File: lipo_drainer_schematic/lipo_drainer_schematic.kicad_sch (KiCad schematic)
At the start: 57 parts, among them J1 BATT, J2 FAN, J3 Vcal, J4 128x64_OLED, J5 Gcal, J6 Ical, Q1 MMBT3904, Q10 G700P06T, Q11 G700P06T, Q2 IRLML5103TRPBF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

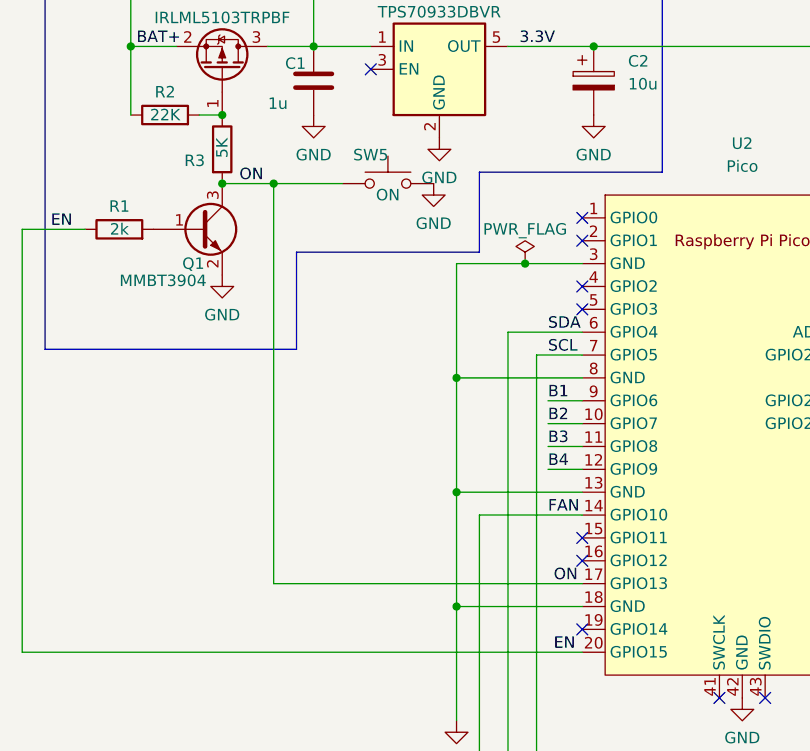
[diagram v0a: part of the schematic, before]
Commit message: Removed ineffective ON button
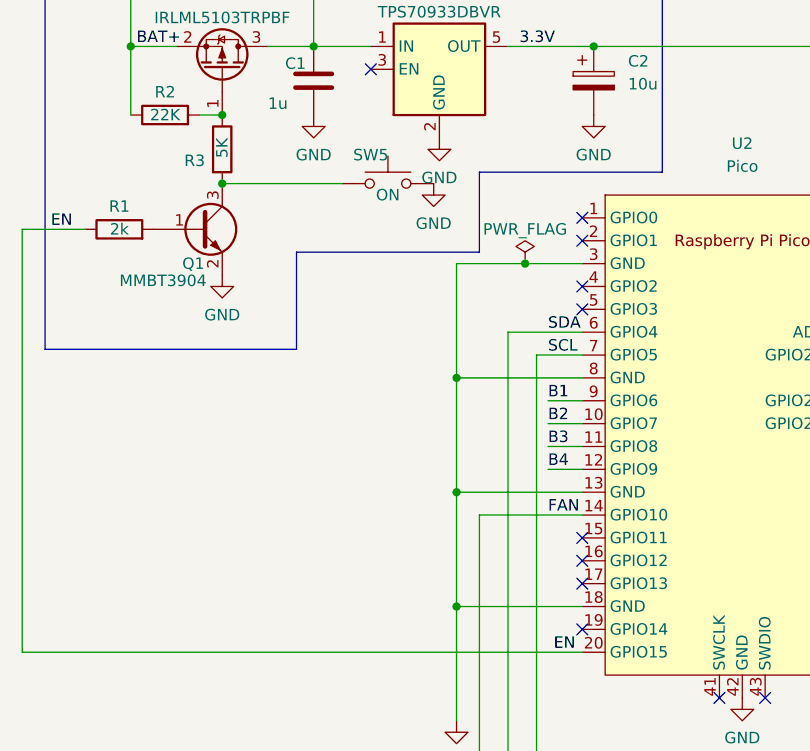
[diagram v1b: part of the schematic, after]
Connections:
- net ON: no longer names the net of Q1.3 (C), R3.2, SW5.1
- net ON: no longer U2.17 (GPIO13)
- no-connect marks 18 -> 19
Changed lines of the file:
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@@
   (junction (at 144.145 118.11) (diameter 0) (color 0 0 0 0)
-  )
-  (junction (at 72.39 71.12) (diameter 0) (color 0 0 0 0)
   )
   (junction (at 258.445 59.055) (diameter 0) (color 0 0 0 0)
@@
   (no_connect (at 142.24 102.87))
   (no_connect (at 142.24 90.17))
+  (no_connect (at 106.68 115.57))
   (no_connect (at 127 128.27))
   (no_connect (at 106.68 113.03))
@@
     (stroke (width 0) (type default))
   )
-  (wire (pts (xy 72.39 115.57) (xy 72.39 71.12))
-    (stroke (width 0) (type default))
-  )
   (polyline (pts (xy 193.675 93.98) (xy 240.665 93.98))
     (stroke (width 0) (type default))
@@
     (stroke (width 0) (type default))
   )
-  (wire (pts (xy 72.39 71.12) (xy 80.01 71.12))
+  (wire (pts (xy 66.675 71.12) (xy 80.01 71.12))
     (stroke (width 0) (type default))
   )
@@
     (stroke (width 0) (type default))
   )
-  (wire (pts (xy 106.68 115.57) (xy 72.39 115.57))
-    (stroke (width 0) (type default))
-  )
   (wire (pts (xy 174.625 39.37) (xy 174.625 43.815))
     (stroke (width 0) (type default))
@@
   )
   (wire (pts (xy 144.145 118.11) (xy 142.24 118.11))
-    (stroke (width 0) (type default))
-  )
-  (wire (pts (xy 66.675 71.12) (xy 72.39 71.12))
     (stroke (width 0) (type default))
   )
@@
     (effects (font (size 1.27 1.27)) (justify left bottom))
   )
-  (label "ON" (at 68.58 71.12 0) (fields_autoplaced)
-    (effects (font (size 1.27 1.27)) (justify left bottom))
-  )
   (label "BAT+" (at 57.15 55.88 0) (fields_autoplaced)
     (effects (font (size 1.27 1.27)) (justify left bottom))
@@
     (effects (font (size 1.27 1.27)) (justify left bottom))
   )
-  (label "ON" (at 103.505 115.57 0) (fields_autoplaced)
-    (effects (font (size 1.27 1.27)) (justify left bottom))
-  )

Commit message: Started work on layout
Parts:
- added R25: 100k, Resistor_SMD:R_0805_2012Metric_Pad1.20x1.40mm_HandSolder, symbol Device:R
- J1: footprint (none) -> Connector_AMASS:AMASS_XT60-M_1x02_P7.20mm_Vertical
- U2: footprint RPi_Pico:RPi_Pico_SMD_TH -> MCU_RaspberryPi_and_Boards:RPi_Pico_SMD_TH
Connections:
- net GND: now also R25.1
- net at C4.1, J5.2 (Pin_2), Q10.1 (G)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: now also R25.2
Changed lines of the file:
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@@
   (junction (at 258.445 59.055) (diameter 0) (color 0 0 0 0)
+  )
+  (junction (at 253.365 66.675) (diameter 0) (color 0 0 0 0)
   )
   (junction (at 127 43.815) (diameter 0) (color 0 0 0 0)
@@
       (effects (font (size 1.27 1.27)) (justify right))
     )
-    (property "Footprint" "" (at 24.13 29.845 0)
+    (property "Footprint" "Connector_AMASS:AMASS_XT60-M_1x02_P7.20mm_Vertical" (at 24.13 29.845 0)
       (effects (font (size 1.27 1.27)) hide)
     )
@@
         (path "/db6692d0-0595-40e8-a350-9f6ef4d6e67d"
           (reference "#PWR06") (unit 1)
+        )
+      )
+    )
+  )
+  (symbol (lib_id "power:GND") (at 253.365 74.295 0) (unit 1)
+    (in_bom yes) (on_board yes) (dnp no) (fields_autoplaced)
+    (property "Reference" "#PWR018" (at 253.365 80.645 0)
+      (effects (font (size 1.27 1.27)) hide)
+    )
+    (property "Value" "GND" (at 253.365 78.74 0)
+      (effects (font (size 1.27 1.27)))
+    )
+    (property "Footprint" "" (at 253.365 74.295 0)
+      (effects (font (size 1.27 1.27)) hide)
+    )
+    (property "Datasheet" "" (at 253.365 74.295 0)
+      (effects (font (size 1.27 1.27)) hide)
+    )
+    (pin "1")
+    (instances
+      (project "lipo_drainer_schematic"
+        (path "/db6692d0-0595-40e8-a350-9f6ef4d6e67d"
+          (reference "#PWR018") (unit 1)
         )
       )
@@
       (effects (font (size 1.27 1.27)))
     )
-    (property "Footprint" "RPi_Pico:RPi_Pico_SMD_TH" (at 124.46 99.06 90)
+    (property "Footprint" "MCU_RaspberryPi_and_Boards:RPi_Pico_SMD_TH" (at 124.46 99.06 90)
       (effects (font (size 1.27 1.27)) hide)
     )
@@
         )
       )
+    )
+  )
+  (symbol (lib_id "Device:R") (at 253.365 70.485 180) (unit 1)
+    (in_bom yes) (on_board yes) (dnp no)
+    (property "Reference" "R25" (at 250.825 70.485 90)
+      (effects (font (size 1.27 1.27)))
+    )
+    (property "Value" "100k" (at 253.365 70.485 90)
+      (effects (font (size 1.27 1.27)))
+    )
+    (property "Footprint" "Resistor_SMD:R_0805_2012Metric_Pad1.20x1.40mm_HandSolder" (at 255.143 70.485 90)
+      (effects (font (size 1.27 1.27)) hide)
+    )
+    (property "Datasheet" "~" (at 253.365 70.485 0)
+      (effects (font (size 1.27 1.27)) hide)
+    )
+    (pin "1")
+    (pin "2")
+    (instances
+      (project "lipo_drainer_schematic"
+        (path "/db6692d0-0595-40e8-a350-9f6ef4d6e67d"
+          (reference "R25") (unit 1)
+        )
+      )

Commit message: Added temperature sensor
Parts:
- added J7: Heatsink Temp (for MCP7901), Connector_PinHeader_2.54mm:PinHeader_1x03_P2.54mm_Vertical, symbol Connector:Conn_01x03_Pin
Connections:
- net GND: now also J7.1 (Pin_1)
- net 3V3: now reaches R7.2, U2.36 (3V3)
- net 3V3: now also J4.1 (Pin_1), J7.2 (Pin_2)
- net TEMP: now reaches U2.34 (GPIO28_ADC2)
- net TEMP: now also J7.3 (Pin_3)
- net 3.3V renamed VSYS
- net VSYS: no longer J4.1 (Pin_1)
- net ADC renamed VOLT
- no-connect marks 19 -> 18
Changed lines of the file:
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@@
   (no_connect (at 83.185 58.42))
   (no_connect (at 142.24 102.87))
-  (no_connect (at 142.24 90.17))
   (no_connect (at 106.68 115.57))
   (no_connect (at 127 128.27))
@@
     (stroke (width 0) (type default))
   )
+  (wire (pts (xy 150.495 90.17) (xy 150.495 133.35))
+    (stroke (width 0) (type default))
+  )
   (wire (pts (xy 225.425 66.675) (xy 238.76 66.675))
     (stroke (width 0) (type default))
@@
     (stroke (width 0) (type default))
   )
+  (wire (pts (xy 150.495 135.89) (xy 154.94 135.89))
+    (stroke (width 0) (type default))
+  )
   (wire (pts (xy 138.43 162.56) (xy 149.86 162.56))
     (stroke (width 0) (type default))
@@
     (stroke (width 0) (type default))
   )
+  (wire (pts (xy 142.24 90.17) (xy 150.495 90.17))
+    (stroke (width 0) (type default))
+  )
   (wire (pts (xy 138.43 160.02) (xy 138.43 162.56))
     (stroke (width 0) (type default))
@@
   )
   (wire (pts (xy 92.71 118.11) (xy 92.71 130.81))
+    (stroke (width 0) (type default))
+  )
+  (wire (pts (xy 150.495 133.35) (xy 154.94 133.35))
     (stroke (width 0) (type default))
   )
@@
     (effects (font (size 1.27 1.27)) (justify left bottom))
   )
-  (label "3.3V" (at 149.225 77.47 0) (fields_autoplaced)
+  (label "VSYS" (at 146.05 77.47 0) (fields_autoplaced)
     (effects (font (size 1.27 1.27)) (justify left bottom))
   )
@@
     (effects (font (size 1.27 1.27)) (justify left bottom))
   )
-  (label "ADC" (at 178.435 67.945 0) (fields_autoplaced)
+  (label "VOLT" (at 178.435 67.945 0) (fields_autoplaced)
     (effects (font (size 1.27 1.27)) (justify left bottom))
   )
@@
     (effects (font (size 1.27 1.27)) (justify left bottom))
   )
-  (label "FAST" (at 146.685 123.19 0) (fields_autoplaced)
+  (label "FAST" (at 144.78 123.19 0) (fields_autoplaced)
     (effects (font (size 1.27 1.27)) (justify left bottom))
   )
@@
     (effects (font (size 1.27 1.27)) (justify left bottom))
   )
-  (label "ADC" (at 149.86 97.79 0) (fields_autoplaced)
+  (label "VOLT" (at 149.225 97.79 0) (fields_autoplaced)
     (effects (font (size 1.27 1.27)) (justify left bottom))
   )
@@
     (effects (font (size 1.27 1.27)) (justify left bottom))
   )
+  (label "TEMP" (at 145.415 90.17 0) (fields_autoplaced)
+    (effects (font (size 1.27 1.27)) (justify left bottom))
+  )
   (label "EN" (at 103.505 123.19 0) (fields_autoplaced)
     (effects (font (size 1.27 1.27)) (justify left bottom))
@@
     (effects (font (size 1.27 1.27)) (justify left bottom))
   )
+  (label "3V3" (at 145.415 85.09 0) (fields_autoplaced)
+    (effects (font (size 1.27 1.27)) (justify left bottom))
+  )
   (label "B1" (at 102.87 95.25 0) (fields_autoplaced)
     (effects (font (size 1.27 1.27)) (justify left bottom))
   )
-  (label "SLOW" (at 146.685 120.65 0) (fields_autoplaced)
+  (label "TEMP" (at 150.495 133.35 0) (fields_autoplaced)
+    (effects (font (size 1.27 1.27)) (justify left bottom))
+  )
+  (label "SLOW" (at 144.78 120.65 0) (fields_autoplaced)
     (effects (font (size 1.27 1.27)) (justify left bottom))
   )
@@
     (effects (font (size 1.27 1.27)) (justify left bottom))
   )
+  (label "3V3" (at 150.495 135.89 0) (fields_autoplaced)
+    (effects (font (size 1.27 1.27)) (justify left bottom))
+  )
   (label "3V" (at 151.13 87.63 0) (fields_autoplaced)
     (effects (font (size 1.27 1.27)) (justify left bottom))
@@
     (effects (font (size 1.27 1.27)) (justify left bottom))
   )
-  (label "3.3V" (at 99.695 55.88 0) (fields_autoplaced)
-    (effects (font (size 1.27 1.27)) (justify left bottom))
-  )
-  (label "3.3V" (at 219.075 135.255 0) (fields_autoplaced)
+  (label "VSYS" (at 99.695 55.88 0) (fields_autoplaced)
+    (effects (font (size 1.27 1.27)) (justify left bottom))
+  )
+  (label "3V3" (at 219.075 135.255 0) (fields_autoplaced)
     (effects (font (size 1.27 1.27)) (justify left bottom))
   )
@@
         (path "/db6692d0-0595-40e8-a350-9f6ef4d6e67d"
           (reference "Q7") (unit 1)
+        )
+      )
+    )
+  )
+  (symbol (lib_id "Connector:Conn_01x03_Pin") (at 160.02 135.89 180) (unit 1)
+    (in_bom yes) (on_board yes) (dnp no) (fields_autoplaced)
+    (property "Reference" "J7" (at 161.29 135.255 0)
+      (effects (font (size 1.27 1.27)) (justify right))
+    )
+    (property "Value" "Heatsink Temp (for MCP7901)" (at 161.29 137.795 0)
+      (effects (font (size 1.27 1.27)) (justify right))
+    )
+    (property "Footprint" "Connector_PinHeader_2.54mm:PinHeader_1x03_P2.54mm_Vertical" (at 160.02 135.89 0)
+      (effects (font (size 1.27 1.27)) hide)
+    )
+    (property "Datasheet" "~" (at 160.02 135.89 0)
+      (effects (font (size 1.27 1.27)) hide)
+    )
+    (pin "1")
+    (pin "2")
+    (pin "3")
+    (instances
+      (project "lipo_drainer_schematic"
+        (path "/db6692d0-0595-40e8-a350-9f6ef4d6e67d"
+          (reference "J7") (unit 1)
         )
       )
@@
     )
   )
-  (symbol (lib_id "power:PWR_FLAG") (at 148.59 87.63 180) (unit 1)
+  (symbol (lib_id "power:PWR_FLAG") (at 148.59 87.63 0) (unit 1)
     (in_bom yes) (on_board yes) (dnp no) (fields_autoplaced)
-    (property "Reference" "#FLG02" (at 148.59 89.535 0)
-      (effects (font (size 1.27 1.27)) hide)
-    )
-    (property "Value" "PWR_FLAG" (at 148.59 92.71 0)
-      (effects (font (size 1.27 1.27)))
+    (property "Reference" "#FLG02" (at 148.59 85.725 0)
+      (effects (font (size 1.27 1.27)) hide)
+    )
+    (property "Value" "PWR_FLAG" (at 151.13 86.995 0)
+      (effects (font (size 1.27 1.27)) (justify left))
     )
     (property "Footprint" "" (at 148.59 87.63 0)
@@
         )
       )
+    )
+  )
+  (symbol (lib_id "power:GND") (at 154.94 138.43 0) (unit 1)
+    (in_bom yes) (on_board yes) (dnp no) (fields_autoplaced)
+    (property "Reference" "#PWR026" (at 154.94 144.78 0)
+      (effects (font (size 1.27 1.27)) hide)
+    )
+    (property "Value" "GND" (at 154.94 142.875 0)
+      (effects (font (size 1.27 1.27)))
+    )
+    (property "Footprint" "" (at 154.94 138.43 0)
+      (effects (font (size 1.27 1.27)) hide)
+    )
+    (property "Datasheet" "" (at 154.94 138.43 0)
+      (effects (font (size 1.27 1.27)) hide)
+    )
+    (pin "1")
+    (instances
+      (project "lipo_drainer_schematic"
+        (path "/db6692d0-0595-40e8-a350-9f6ef4d6e67d"
+          (reference "#PWR026") (unit 1)
+        )
+      )
